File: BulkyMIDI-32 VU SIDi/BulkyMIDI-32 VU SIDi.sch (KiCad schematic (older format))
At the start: 108 parts, among them J1 DC IN, J12 SERIAL, J13 ICSP, J2 MIDI THRU, J3 MIDI IN, J4 Panel, J5 VU INPUT, J6 PWR, J7 PWR, J8 SID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

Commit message: Untested VU SIDI module
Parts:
- removed J7: PWR, symbol Connector_Generic:Conn_01x02
- removed RV1, RV2: 10k, symbol Device:R_POT
- removed RV3, RV4: VOL_R, symbol Device:R_POT
- added RV1: LUM, RK097G:RK097G, symbol Device:R_POT_Dual_Separate
- added RV3: VOL, RK097G:RK097G, symbol Device:R_POT_Dual_Separate
- C13, C14, C15, C16, C19, C2, C20, C21, C22, C4, C5, C8: footprint Capacitor_THT:CP_Radial_D8.0mm_P3.50mm -> Capacitor_THT:CP_Radial_D4.0mm_P2.00mm
- C18, C24: footprint Capacitor_THT:CP_Radial_D8.0mm_P3.50mm -> Capacitor_THT:CP_Radial_D6.3mm_P2.50mm
- J4: footprint BulkyMIDI-32:Channel_Panel -> BulkyMIDI-32:VU_SIDI_Panel
- J5, J8, J9: footprint (none) -> audio_jack:Tayda_3.5mm_stereo_TRS_jack_A-853
- J6: value PWR -> Power; footprint (none) -> BulkyMIDI-32:Conn_Power; symbol Connector_Generic:Conn_01x02 -> BulkyMIDI:Conn_Power
- JP1, JP2: footprint (none) -> Connector_PinHeader_2.54mm:PinHeader_1x02_P2.54mm_Vertical
- JP3, JP4: footprint (none) -> Connector_PinHeader_2.54mm:PinHeader_1x03_P2.54mm_Vertical
- JP5, JP6: footprint (none) -> Jumper:SolderJumper-2_P1.3mm_Open_Pad1.0x1.5mm
- Q1, Q2, Q3: footprint Package_TO_SOT_THT:TO-92_Inline -> Package_TO_SOT_THT:TO-92_Inline_Wide
- R1, R17, R18, R19, R2, R20, R21: footprint Resistor_THT:R_Axial_DIN0207_L6.3mm_D2.5mm_P10.16mm_Horizontal -> resistor:R_Axial_DIN0207_L6.3mm_D2.5mm_P10.16mm_Horizontal
- R10, R11, R12, R13, R14, R15, R16, R3, R4, R5, R6, R7, R8, R9: footprint (none) -> resistor:R_Axial_DIN0207_L6.3mm_D2.5mm_P10.16mm_Horizontal
- SW1: footprint Button_Switch_THT:SW_Tactile_SPST_Angled_PTS645Vx39-2LFS -> Button_Switch_THT:SW_PUSH_6mm
- U1: footprint Package_DIP:DIP-16_W7.62mm_Socket_LongPads -> Package_DIP:DIP-14_W7.62mm_Socket_LongPads
- U2, U4: footprint (none) -> Package_DIP:DIP-18_W7.62mm_Socket_LongPads
- U5, U8: footprint (none) -> Package_DIP:DIP-28_W15.24mm_Socket_LongPads
- U7, U9: footprint (none) -> Package_DIP:DIP-8_W7.62mm_Socket_LongPads
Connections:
- net GND: now also RV1.1, RV1.2, RV1.4, RV1.5, RV3.1, RV3.4
- net at C5.1, R6.1, U2.5 (SIG): now also RV1.3
- net at C8.1, R11.1, U4.5 (SIG): now also RV1.6
- net at C13.2: now also RV3.3
- net at U7.3 (+): now also RV3.2
- net at C19.2: now also RV3.6
- net at U9.3 (+): now also RV3.5

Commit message: Increase C4/C16 capacity slightly
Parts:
- C16, C4: value 1uF -> 10uF
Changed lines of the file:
@@
 P 9175 9650
 F 0 "C16" H 9000 9725 50  0000 C CNN
-F 1 "1uF" H 9000 9650 50  0000 C CNN
+F 1 "10uF" H 9000 9650 50  0000 C CNN
 F 2 "Capacitor_THT:CP_Radial_D4.0mm_P2.00mm" H 9175 9650 50  0001 C CNN
 F 3 "~" H 9175 9650 50  0001 C CNN
@@
 P 5225 9650
 F 0 "C4" H 5050 9725 50  0000 C CNN
-F 1 "1uF" H 5050 9650 50  0000 C CNN
+F 1 "10uF" H 5050 9650 50  0000 C CNN
 F 2 "Capacitor_THT:CP_Radial_D4.0mm_P2.00mm" H 5225 9650 50  0001 C CNN
 F 3 "~" H 5225 9650 50  0001 C CNN

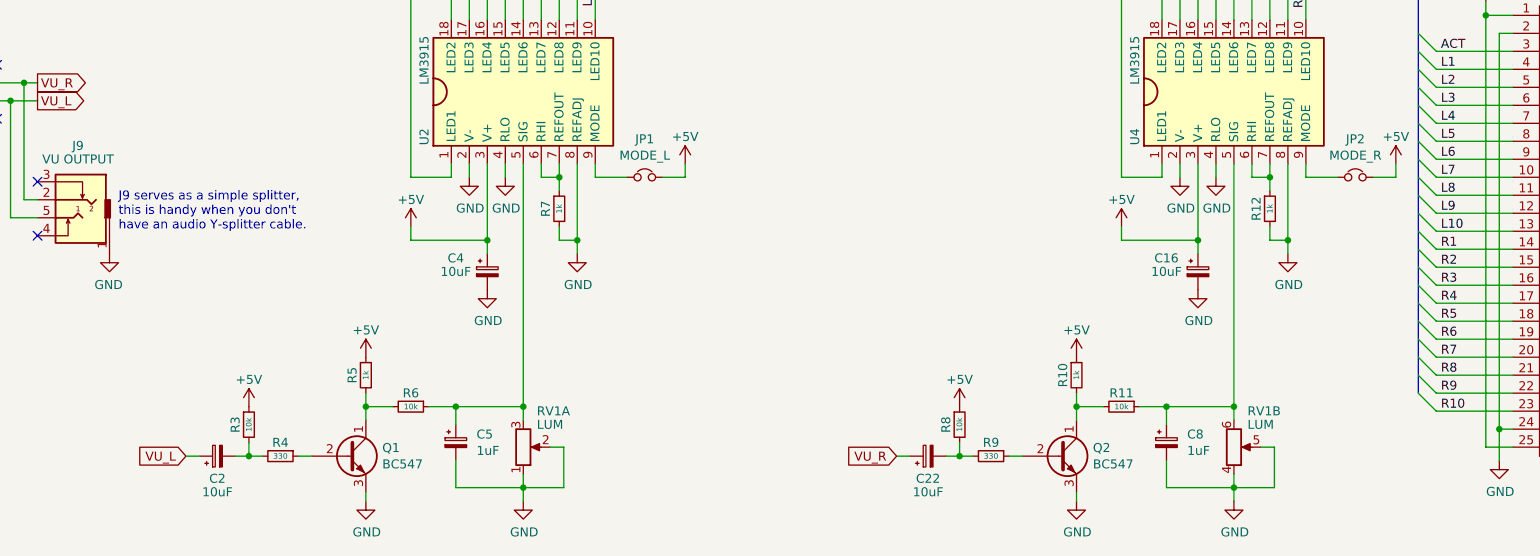
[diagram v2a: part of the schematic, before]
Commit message: Simpler VU meter circuit
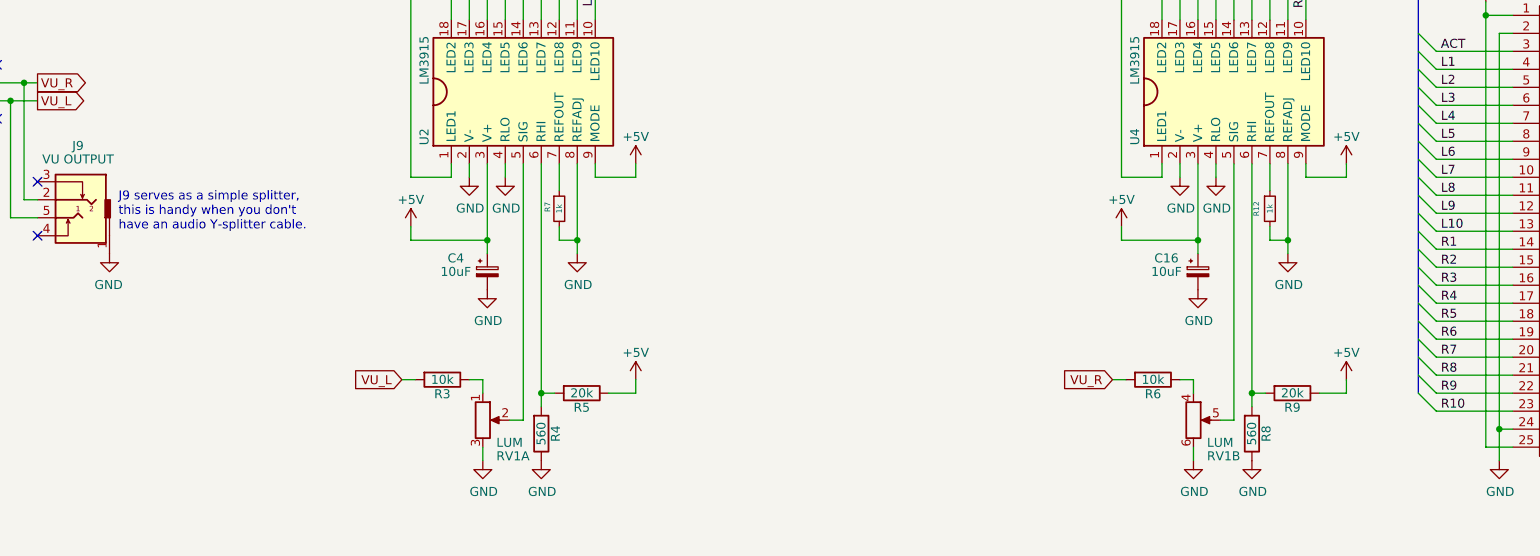
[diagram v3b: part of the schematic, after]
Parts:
- removed C2, C22: 10uF, Capacitor_THT:CP_Radial_D4.0mm_P2.00mm, symbol Device:CP_Small
- removed C5, C8: 1uF, Capacitor_THT:CP_Radial_D4.0mm_P2.00mm, symbol Device:CP_Small
- removed JP1: MODE_L, Connector_PinHeader_2.54mm:PinHeader_1x02_P2.54mm_Vertical, symbol Device:Jumper_NC_Small
- removed JP2: MODE_R, Connector_PinHeader_2.54mm:PinHeader_1x02_P2.54mm_Vertical, symbol Device:Jumper_NC_Small
- removed Q1, Q2: BC547, Package_TO_SOT_THT:TO-92_Inline_Wide, symbol Transistor_BJT:BC547
- removed R10, R5: 1k, resistor:R_Axial_DIN0207_L6.3mm_D2.5mm_P10.16mm_Horizontal, symbol Device:R_Small
- removed R11, R3, R6, R8: 10k, resistor:R_Axial_DIN0207_L6.3mm_D2.5mm_P10.16mm_Horizontal, symbol Device:R_Small
- removed R4, R9: 330, resistor:R_Axial_DIN0207_L6.3mm_D2.5mm_P10.16mm_Horizontal, symbol Device:R_Small
- added R3, R6: 10k, resistor:R_Axial_DIN0207_L6.3mm_D2.5mm_P10.16mm_Horizontal, symbol Device:R
- added R4, R8: 560, resistor:R_Axial_DIN0207_L6.3mm_D2.5mm_P10.16mm_Horizontal, symbol Device:R
- added R5, R9: 20k, resistor:R_Axial_DIN0207_L6.3mm_D2.5mm_P10.16mm_Horizontal, symbol Device:R
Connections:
- net +5V: now also U2.9 (MODE), U4.9 (MODE), R5.1, R9.1
- net GND: now also RV1.3, RV1.6, R4.1, R8.1; no longer RV1.1, RV1.2, RV1.4, RV1.5
- net VU_L: now also R3.2
- net VU_R: now also R6.2
- net at U2.5 (SIG): now also RV1.2; no longer RV1.3
- net at R7.1, U2.7 (REFOUT): no longer U2.6 (RHI)
- net at U4.5 (SIG): now also RV1.5; no longer RV1.6
- net at R12.1, U4.7 (REFOUT): no longer U4.6 (RHI)
- new net: R3.1, RV1.1
- new net: R6.1, RV1.4
- new net: R4.2, R5.2, U2.6 (RHI)
- new net: R8.2, R9.2, U4.6 (RHI)
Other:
- moved on the sheet: RV1A, RV1B

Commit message: Update connectors
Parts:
- J2: footprint BulkyMIDI-32:DIN5_MIDI -> BulkyMIDI-32:DIN5_MIDI_OUT; symbol Connector:DIN-5_180degree -> BulkyMIDI:DIN-5_MIDI
- J3: footprint BulkyMIDI-32:DIN5_MIDI -> BulkyMIDI-32:DIN5_MIDI_IN; symbol Connector:DIN-5_180degree -> BulkyMIDI:DIN-5_MIDI
- J5: footprint audio_jack:Tayda_3.5mm_stereo_TRS_jack_A-853 -> audio_jack:PJ-317_IN
- J8, J9: footprint audio_jack:Tayda_3.5mm_stereo_TRS_jack_A-853 -> audio_jack:PJ-317_OUT
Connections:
- net GND: now also J2.6
- no-connect marks 31 -> 32
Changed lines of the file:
@@
 $EndComp
 $Comp
-L Connector:DIN-5_180degree J2
+L BulkyMIDI:DIN-5_MIDI J2
 U 1 1 5FBFBE67
 P 1450 2100
 F 0 "J2" H 1450 1733 50  0000 C CNN
 F 1 "MIDI THRU" H 1450 1824 50  0000 C CNN
-F 2 "BulkyMIDI-32:DIN5_MIDI" H 1450 2100 50  0001 C CNN
+F 2 "BulkyMIDI-32:DIN5_MIDI_OUT" H 1450 2100 50  0001 C CNN
 F 3 "" H 1450 2100 50  0001 C CNN
 	1    1450 2100
@@
 L power:GND #PWR012
 U 1 1 5FD12B0A
-P 1450 2475
-F 0 "#PWR012" H 1450 2225 50  0001 C CNN
-F 1 "GND" H 1455 2302 50  0000 C CNN
-F 2 "" H 1450 2475 50  0001 C CNN
-F 3 "" H 1450 2475 50  0001 C CNN
-	1    1450 2475
+P 1450 2550
+F 0 "#PWR012" H 1450 2300 50  0001 C CNN
+F 1 "GND" H 1455 2377 50  0000 C CNN
+F 2 "" H 1450 2550 50  0001 C CNN
+F 3 "" H 1450 2550 50  0001 C CNN
+	1    1450 2550
 	-1   0    0    -1
 $EndComp
@@
 	800  2200 800  2125
 $Comp
-L Connector:DIN-5_180degree J3
+L BulkyMIDI:DIN-5_MIDI J3
 U 1 1 64BE52C1
 P 2075 1050
 F 0 "J3" H 2075 683 50  0000 C CNN
 F 1 "MIDI IN" H 2075 774 50  0000 C CNN
-F 2 "BulkyMIDI-32:DIN5_MIDI" H 2075 1050 50  0001 C CNN
+F 2 "BulkyMIDI-32:DIN5_MIDI_IN" H 2075 1050 50  0001 C CNN
 F 3 "" H 2075 1050 50  0001 C CNN
 	1    2075 1050
@@
 $EndComp
 Wire Wire Line
-	1450 2400 1450 2475
+	1450 2475 1450 2550
 $Comp
 L Device:R R1
@@
 F 0 "J5" H 2275 9100 50  0000 C CNN
 F 1 "VU INPUT" H 2275 9025 50  0000 C CNN
-F 2 "audio_jack:Tayda_3.5mm_stereo_TRS_jack_A-853" H 2550 8800 50  0001 C CNN
+F 2 "audio_jack:PJ-317_IN" H 2550 8800 50  0001 C CNN
 F 3 "~" H 2550 8800 50  0001 C CNN
 	1    2300 8700
@@
 F 0 "J8" H 15678 4550 50  0000 C CNN
 F 1 "SID" H 15678 4459 50  0000 C CNN
-F 2 "audio_jack:Tayda_3.5mm_stereo_TRS_jack_A-853" H 15950 4225 50  0001 C CNN
+F 2 "audio_jack:PJ-317_OUT" H 15950 4225 50  0001 C CNN
 F 3 "~" H 15950 4225 50  0001 C CNN
 	1    15700 4125
@@
 F 0 "J9" H 2900 9750 50  0000 C CNN
 F 1 "VU OUTPUT" H 2900 9675 50  0000 C CNN
-F 2 "audio_jack:Tayda_3.5mm_stereo_TRS_jack_A-853" H 3175 9450 50  0001 C CNN
+F 2 "audio_jack:PJ-317_OUT" H 3175 9450 50  0001 C CNN
 F 3 "~" H 3175 9450 50  0001 C CNN
 	1    2925 9350
@@
 Wire Wire Line
 	9850 10325 10000 10325
+NoConn ~ 2175 1325
+Wire Wire Line
+	1450 2475 1350 2475
+Wire Wire Line
+	1350 2475 1350 2375
+Wire Wire Line
+	1450 2400 1450 2475
 Wire Bus Line
 	10400 5900 10400 6450
@@
 Wire Bus Line
 	2150 7925 10400 7925
+Connection ~ 1450 2475
 $EndSCHEMATC
